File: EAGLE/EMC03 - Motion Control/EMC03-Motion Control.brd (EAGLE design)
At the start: 100 x 86.6 mm, 136 parts, among them J1 UART0, J10 S4B-PH-SM4, J11 S4B-PH-SM4, J12 S4B-PH-SM4, J13 S5B-PH-SM4, J14 S5B-PH-SM4, J15 S5B-PH-SM4, J17 S8B-PH-SM4, J19 S6B-PH-SM4, J2 FTSH-105-1-L-DV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

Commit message: Replaced switching regulator with a smaller LDO, with smaller accompanying components. Preliminary component placement for EMC03. Partial routing of power nets.
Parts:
- removed C51: 0.47uF, TinWhiskers:C0603
- removed D15: SJPB-H6, TinWhiskers:DIO-SM2
- removed L1: 100uH, TinWhiskers:2020
- removed LOGO8: LOGO-CC-BY-SALARGE, FirePick:LOGO-CC-BY-SA
- removed VR2: SI-8033JD, TinWhiskers:TO263-5
- added VR1: LMS8117AMP-3.3/NOPB, TinWhiskers:SOT-223
- C3: value 220uF -> 10uF
- C4: value 470uF -> 10uF
- U1: device TinWhiskers:LQFP-100 -> TinWhiskers:100-LQFP
- U6, U7, U8: device TinWhiskers:QFN36-(5X6) -> TinWhiskers:36-QFN(5X6)
- moved C20 256.7 mm to (65.5, 60.2)
- moved U3 246.4 mm to (37.3, 30.6)
- moved C21 244.9 mm to (32.4, 66.3)
- moved C22 234.2 mm to (58.2, 22.1)
- moved J17 224.4 mm to (23.9, 24.4), turned to 120 degrees
- moved C11 214.7 mm to (-4.06, 84.7)
- moved C12 214.7 mm to (-4.06, 79.6)
- moved C13 214.7 mm to (-4.06, 74.5)
- moved C14 214.7 mm to (-4.06, 69.5)
- moved C19 214.7 mm to (-4.06, 59.3)
- moved R12 214.7 mm to (-4.57, 88.4)
- moved C18 214.7 mm to (-4.06, 64.4)
- moved R11 188.8 mm to (-11.9, 87.6)
- moved C3 105.9 mm to (57.4, 81.3), turned to 180 degrees
- moved TB1 93.6 mm to (50.5, 91.5)
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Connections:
- removed net N$16: D15.POS, L1.1, VR2.2
- removed net N$17: C51.2, VR2.5
- net +3V3: now also VR1.2; no longer L1.2, VR2.4
- net +5V: now also VR1.3; no longer VR2.1
- net GND: now also VR1.1, VR1.P$1; no longer C51.1, D15.NEG, VR2.3, VR2.GND
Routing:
- net +3V3: track 0.00 -> 91.3 mm, vias 0 -> 2
- net CLK: track 0.00 -> 53.2 mm, vias 0 -> 2
- net DPWR: track 0.00 -> 33.9 mm, vias 0 -> 4
- net XTAL1: track 0.00 -> 24.7 mm, vias 0 -> 2
- net STAT_LED7: track 0.00 -> 22.0 mm, vias 0 -> 2
- net STAT_LED6: track 0.00 -> 21.5 mm, vias 0 -> 2
- net STAT_LED5: track 0.00 -> 19.6 mm, vias 0 -> 2
- net STAT_LED4: track 0.00 -> 17.4 mm, vias 0 -> 2
- net !ENABLE_LPC: track 0.00 -> 17.2 mm, vias 0 -> 2
- net XTAL2: track 0.00 -> 13.7 mm
- net DFU: track 0.00 -> 8.60 mm
- net X_STOP: track 0.00 -> 8.59 mm
- net N$9: track 0.00 -> 1.67 mm
- net X_MIN: track 0.12 -> 1.78 mm
- net N$20: track 0.00 -> 1.65 mm
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- removed copper zone on layer 1, net 12V
- removed copper zone on layer 16, net 12V
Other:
- board text removed: "!RESET"
- board text removed: "!RST"
- board text removed: "20_SDA"
- board text removed: "21_SCL"
- board text removed: "3.3V"
- board text removed: "AREF"
- board text removed: "BOT"
- board text removed: "D13"
- board text removed: "DATA"
- board text removed: "E-STOP"
- board text removed: "FAN2"
- board text removed: "I2C"
- board text removed: "IOREF"
- board text removed: "JTAG"
- board text removed: "MISO"
- board text removed: "MODULAR TOOL #1"
- board text removed: "MODULAR TOOL #2"
- board text removed: "MODULAR TOOL #3"
- board text removed: "MODULAR TOOL #4"
- board text removed: "MOSI"
- board text removed: "RESET"
- board text removed: "RX"
- board text removed: "RX1"
- board text removed: "RX2"
- board text removed: "RX3"
- board text removed: "Released under CC-BY-SA 4.0 license (http://goo.gl/B0gjwG) Design by Neil Jansen"
- board text removed: "SCL"
- board text removed: "SCLK"
- board text removed: "SDA"
- board text removed: "SPI/ISCP"
- board text removed: "TCK"
- board text removed: "TDI"
- board text removed: "TDO"
- board text removed: "TMS"
- board text removed: "TOP"
- board text removed: "TX"
- board text removed: "TX1"
- board text removed: "TX2"
- board text removed: "TX3"
- board text removed: "TXD"
- board text removed: "VIN"

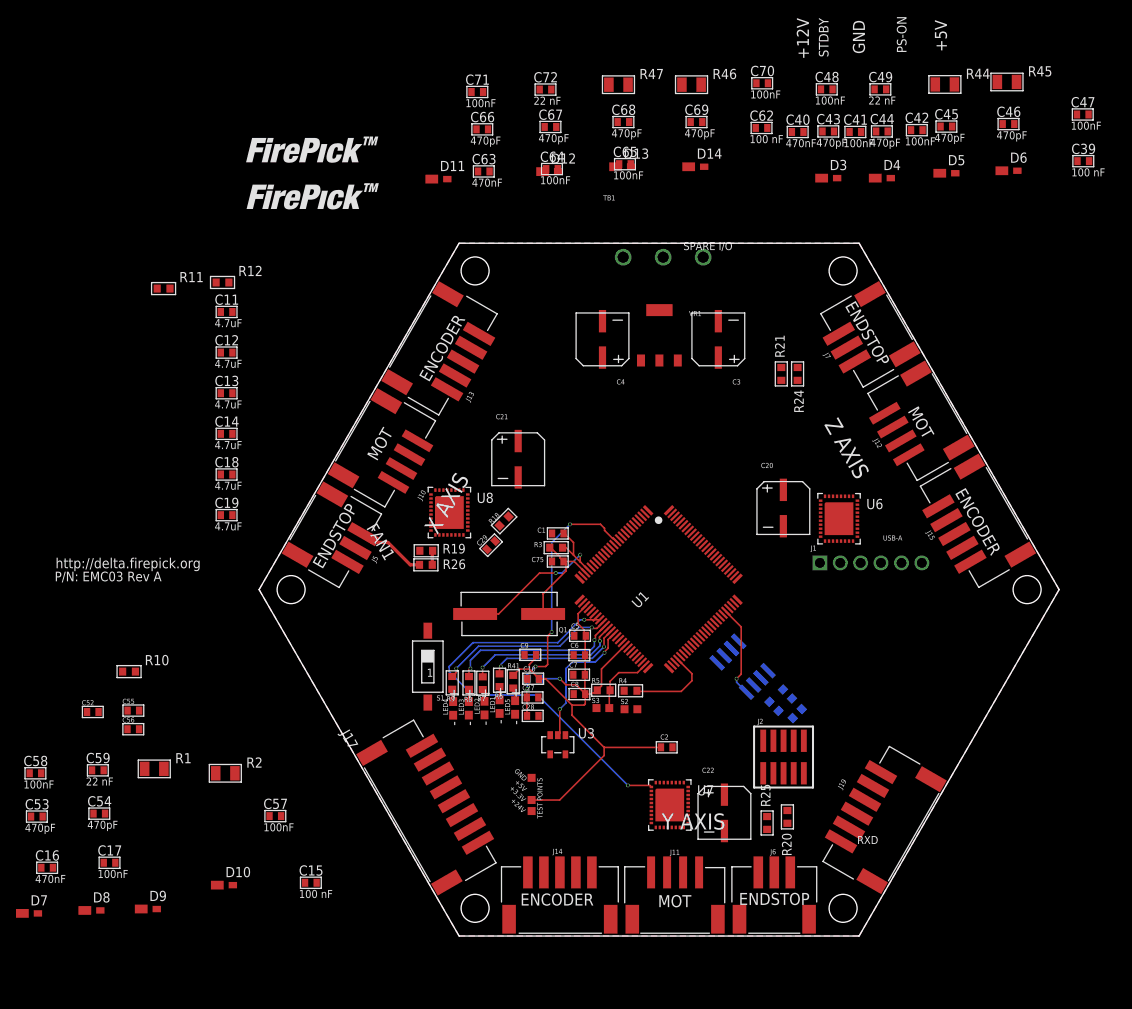
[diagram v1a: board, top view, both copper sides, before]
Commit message: All parts placed for EMC03, X Axis routed.
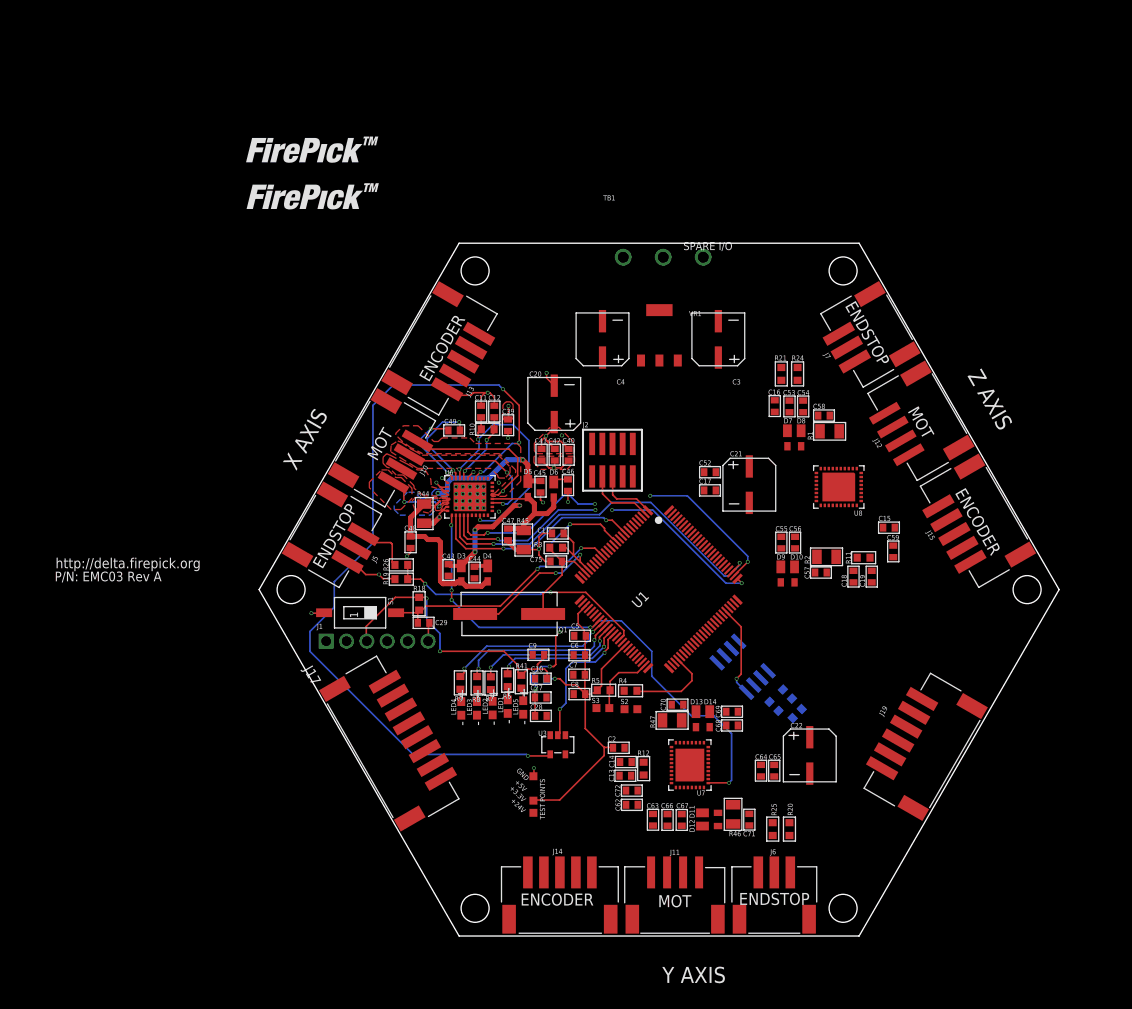
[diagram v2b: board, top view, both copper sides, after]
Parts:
- moved D7 111.8 mm to (66.0, 69.0), turned to 270 degrees
- moved C58 108.2 mm to (70.6, 71.8)
- moved C16 107.7 mm to (64.5, 72.9), turned to 90 degrees
- moved C53 107.1 mm to (66.3, 72.9), turned to 90 degrees
- moved D8 106.5 mm to (67.8, 69.0), turned to 270 degrees
- moved C59 103.1 mm to (79.3, 54.8), turned to 90 degrees
- moved C54 101.6 mm to (68.0, 72.9), turned to 90 degrees
- moved C71 97.1 mm to (61.3, 21.2), turned to 90 degrees
- moved R1 94.4 mm to (71.3, 69.8)
- moved R11 93.7 mm to (75.6, 54.0), turned to 180 degrees
- moved R46 91.4 mm to (59.2, 21.9), turned to 90 degrees
- moved D9 89.5 mm to (65.2, 51.9), turned to 270 degrees
- moved C66 89.4 mm to (51.1, 21.2), turned to 270 degrees
- moved C47 89.0 mm to (31.1, 56.9), turned to 270 degrees
- moved C17 88.3 mm to (56.4, 62.4)
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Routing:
- net !ENABLE: track 0.00 -> 102.0 mm, vias 0 -> 4
- net GND: track 0.00 -> 46.7 mm, vias 0 -> 20
- net SCK: track 0.00 -> 46.5 mm, vias 0 -> 2
- net MISO: track 0.00 -> 46.4 mm, vias 0 -> 4
- net MOSI: track 0.00 -> 43.7 mm, vias 0 -> 4
- net 2B_1: track 0.00 -> 37.7 mm, vias 0 -> 4
- net RESET: track 0.00 -> 31.4 mm, vias 0 -> 2
- net N$1: track 0.00 -> 31.3 mm, vias 0 -> 3
- net X_MIN: track 1.78 -> 33.0 mm, vias 0 -> 2
- net SPI_!CS1: track 0.00 -> 27.0 mm, vias 0 -> 2
- net 2A_1: track 0.00 -> 21.2 mm, vias 0 -> 2
- net BRA: track 0.00 -> 20.3 mm
- net 1A_1: track 0.00 -> 18.2 mm, vias 0 -> 2
- net BRB: track 0.00 -> 16.1 mm
- net +3V3: track 91.3 -> 106.9 mm, vias 2 -> 4
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- added copper zone on layer 1, net +24V
- added copper zone on layer 15, net +24V
- added copper zone on layer 1, net 1A_1
- added copper zone on layer 16, net 1A_1
- added copper zone on layer 1, net 1B_1
- added copper zone on layer 16, net 1B_1
- added copper zone on layer 1, net 2A_1
- added copper zone on layer 1, net 2B_1
- added copper zone on layer 1, net BRA
- added copper zone on layer 2, net GND
- removed copper zone on layer 16, net GND
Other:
- board text removed: "+12V"
- board text removed: "FAN1"
- board text removed: "PS-ON"
- board text removed: "RXD"
- board text removed: "STDBY"
- board text removed: "USB-A"

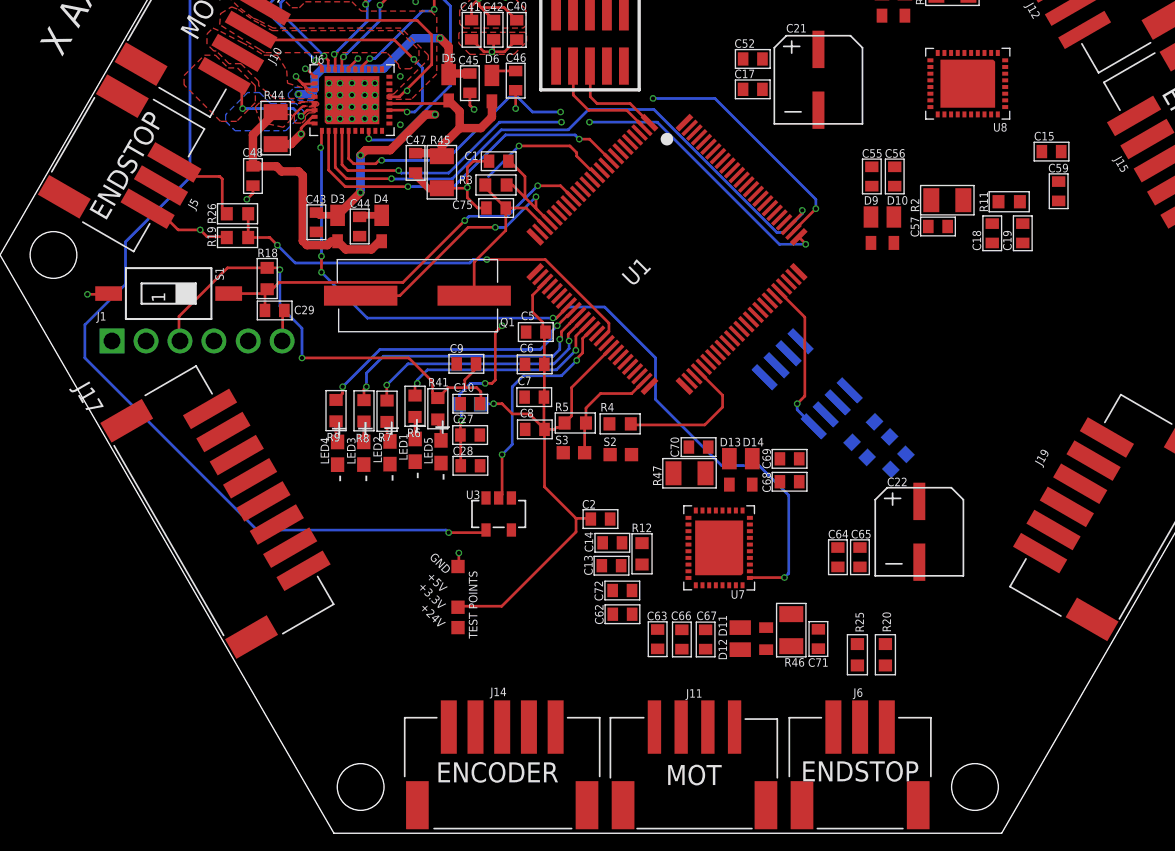
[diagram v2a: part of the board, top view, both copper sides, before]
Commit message: Routed EFD01, ECAM03 boards. Modification needs to be made for hole/keepout in ECAM03. EMC03 X and Y sides routed. Will need to increase some trace widths.
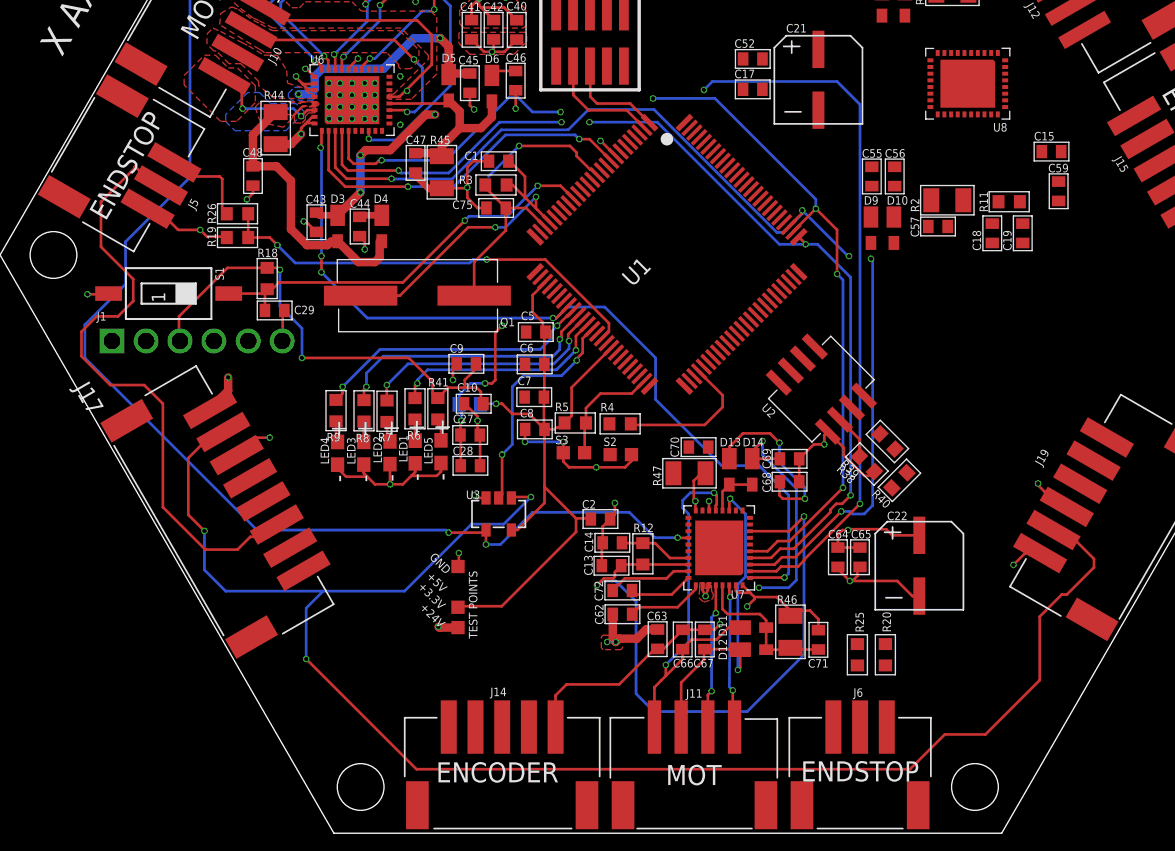
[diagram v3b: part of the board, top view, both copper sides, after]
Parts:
- moved R39 2.83 mm to (64.9, 34.3), flipped to the top, turned to 135 degrees
- moved C22 2.54 mm to (68.8, 26.7)
- moved R38 2.17 mm to (66.4, 36.0), flipped to the top, turned to 315 degrees
- moved R40 1.38 mm to (67.3, 33.1), flipped to the top, turned to 45 degrees
- moved U2 1.13 mm to (61.5, 40.0), flipped to the top, turned to 315 degrees
- moved C10 0.25 mm to (35.5, 38.9)
- moved R6 0.19 mm to (31.1, 38.5)
- moved R46 0.14 mm to (59.2, 21.8), turned to 270 degrees
- moved LED1 0.13 mm to (31.1, 35.2)
- moved R12 0.06 mm to (48.1, 27.6), turned to 270 degrees
- moved C71 0.06 mm to (61.3, 21.2)
- moved C66 0.06 mm to (51.1, 21.2), turned to 90 degrees
- moved C67 0.06 mm to (52.8, 21.2), turned to 90 degrees
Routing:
- net !ENABLE_MOD: track 0.00 -> 123.5 mm, vias 0 -> 3
- net GND: track 46.7 -> 145.0 mm, vias 20 -> 37
- net SPI_!CS2: track 0.00 -> 64.8 mm, vias 0 -> 3
- net N$6: track 0.00 -> 48.0 mm, vias 0 -> 2
- net +5V: track 0.00 -> 47.3 mm
- net SCK: track 46.5 -> 82.9 mm, vias 2 -> 5
- net 1B_2: track 0.00 -> 31.5 mm, vias 0 -> 4
- net MISO: track 46.4 -> 77.1 mm, vias 4 -> 6
- net MOSI: track 43.7 -> 74.0 mm, vias 4 -> 5
- net 2B_2: track 0.00 -> 29.8 mm, vias 0 -> 2
- net 2A_2: track 0.00 -> 25.3 mm, vias 0 -> 2
- net 1A_2: track 0.00 -> 24.2 mm, vias 0 -> 4
- net +24V: track 13.9 -> 37.9 mm, vias 3 -> 11
- net !ENABLE: track 102.0 -> 120.0 mm, vias 4 -> 6
- net BRA2: track 0.00 -> 11.6 mm
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
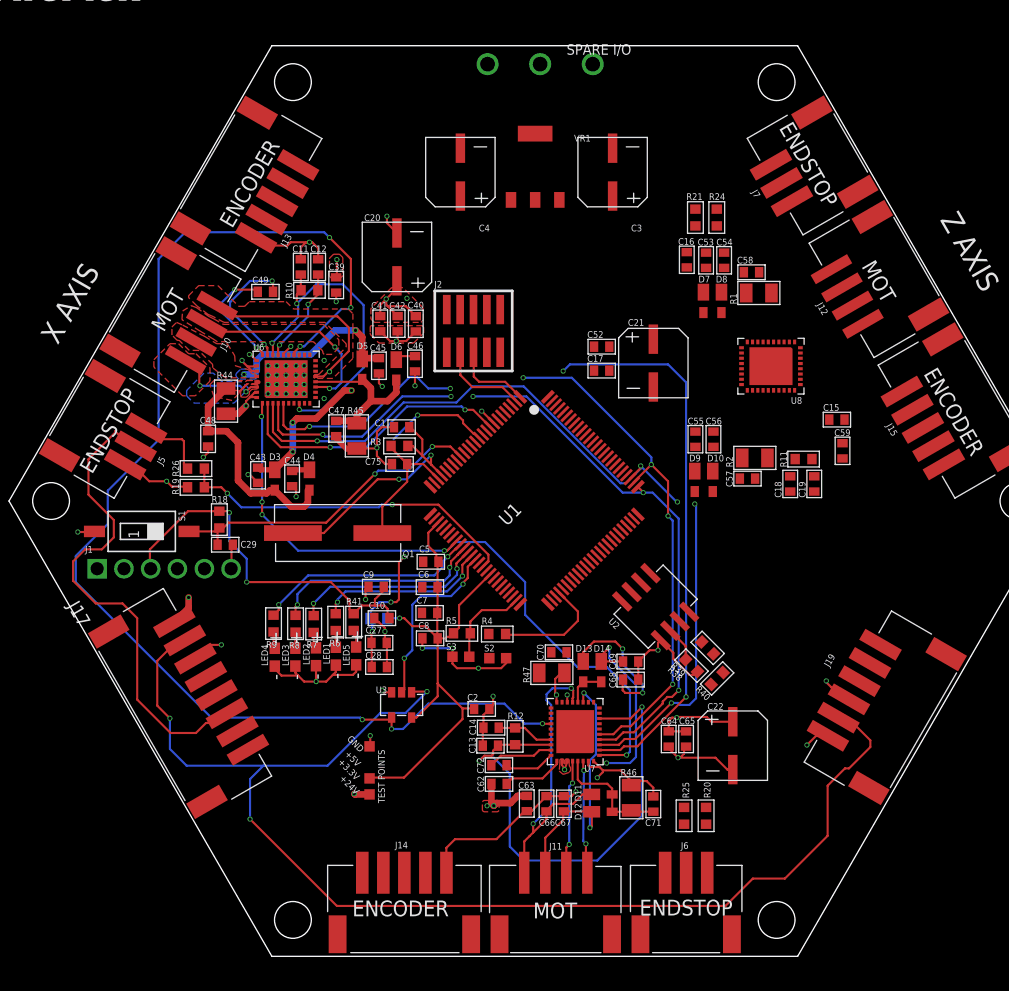
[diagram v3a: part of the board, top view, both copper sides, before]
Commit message: Routing completed for EMC03, need to clean DRC, format. Routing completed for ECAM03.
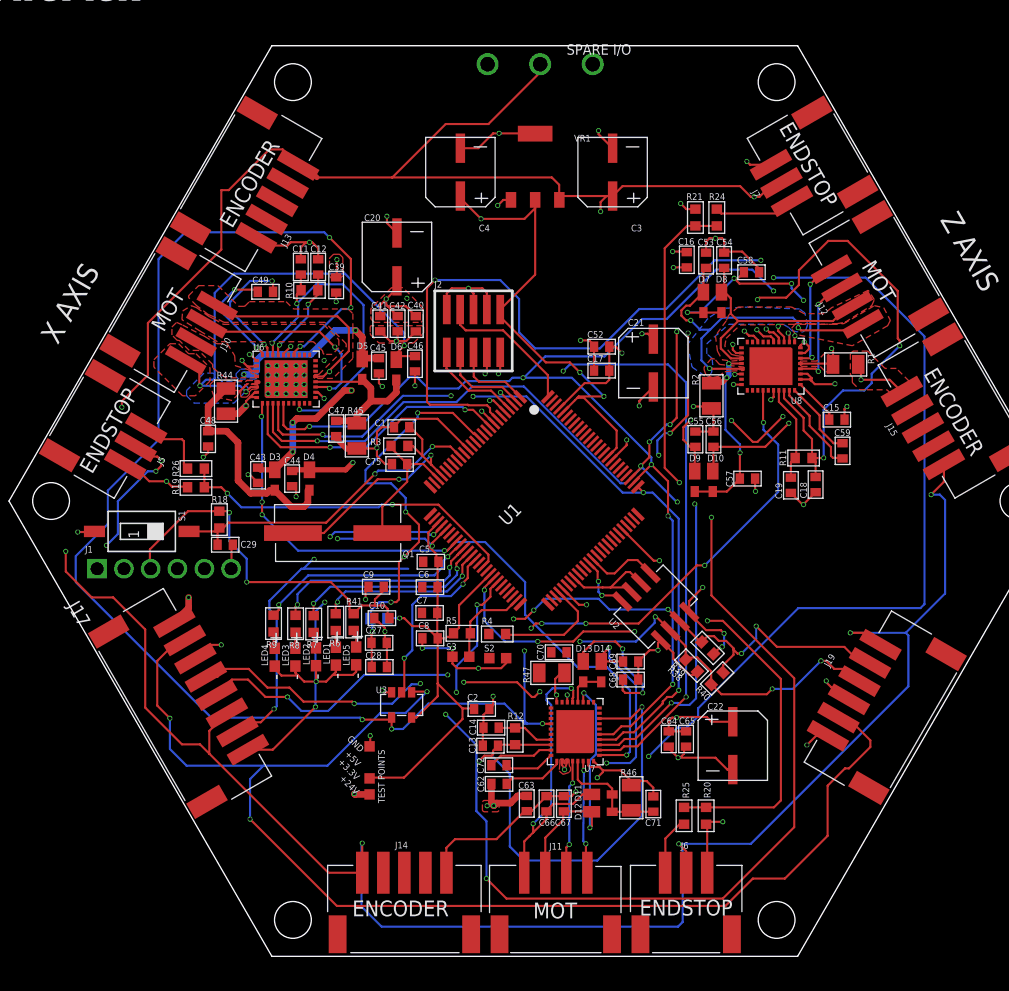
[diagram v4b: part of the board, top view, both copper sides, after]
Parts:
- moved R1 10.7 mm to (79.6, 63.0), turned to 180 degrees
- moved R2 7.20 mm to (66.8, 60.0), turned to 90 degrees
- moved C18 2.41 mm to (76.7, 51.6)
- moved C19 2.23 mm to (74.4, 51.5)
- moved R11 0.10 mm to (75.6, 54.1), turned to 0 degrees
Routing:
- net +5V: track 47.3 -> 291.7 mm, vias 0 -> 11
- net Z_MIN: track 0.00 -> 131.6 mm, vias 0 -> 6
- net GND: track 145.0 -> 236.2 mm, vias 37 -> 58
- net CLK: track 65.6 -> 149.5 mm, vias 5 -> 8
- net B: track 0.00 -> 76.9 mm, vias 0 -> 7
- net A: track 3.36 -> 76.1 mm, vias 0 -> 8
- net SPI_!CS3: track 0.00 -> 68.1 mm, vias 0 -> 3
- net +3V3: track 100.2 -> 166.0 mm, vias 3 -> 10
- net Y_MIN: track 0.00 -> 57.6 mm, vias 0 -> 4
- net N$4: track 0.00 -> 54.5 mm, vias 0 -> 4
- net !ENABLE: track 120.0 -> 168.8 mm, vias 6 -> 12
- net USBMCU+: track 0.00 -> 45.0 mm, vias 0 -> 4
- net USBMCU-: track 0.00 -> 36.4 mm, vias 0 -> 4
- net MISO: track 77.1 -> 112.6 mm, vias 6 -> 7
- net 1B_1: track 10.9 -> 44.7 mm, vias 2 -> 3
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- added copper zone on layer 1, net 2A_3
- added copper zone on layer 1, net 2B_3
- added copper zone on layer 16, net 2B_3
- added copper zone on layer 1, net BRA3
